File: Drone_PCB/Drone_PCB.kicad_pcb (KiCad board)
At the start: 2 copper layers, 36.2 x 36.2 mm, 53 parts, among them J1 Conn_01x02, J2 Conn_01x02, J3 Conn_01x02, J4 Conn_01x02, J5 USB_B_Mini, J6 Conn_01x05, J7 Conn_01x05, J8 Conn_01x05, J9 Conn_01x02, Q1 TRANS_NPN-MMBT2222AL, Q2 TRANS_NPN-MMBT2222AL, U1 ESP32-WROOM-32, U2 CP2104, U3 SI2302-TP, U4 MIC5219-3.3YMM, U5 SI2302-TP, U6 MPU-6050, U8 SI2302-TP, U9 SI2302-TP

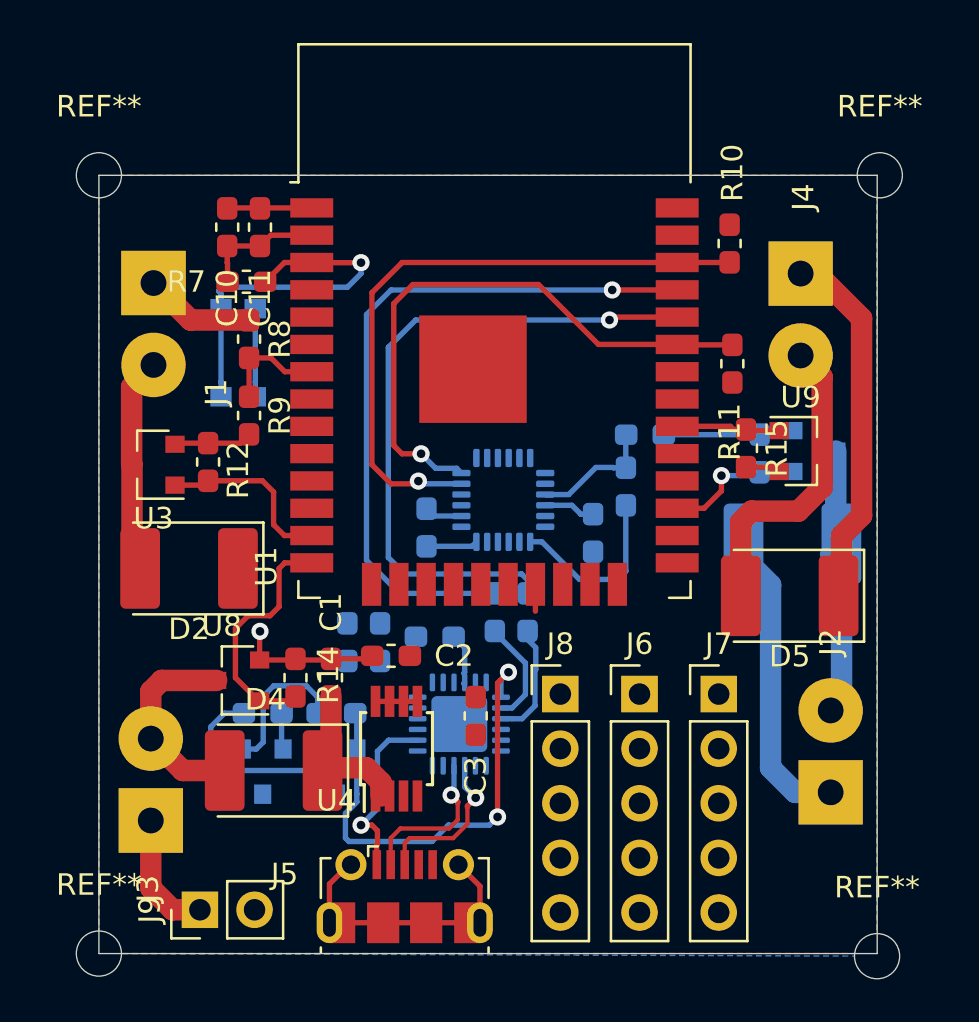
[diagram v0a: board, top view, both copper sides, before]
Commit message: Routing Part 6
We made the tracks thicker and removed some components
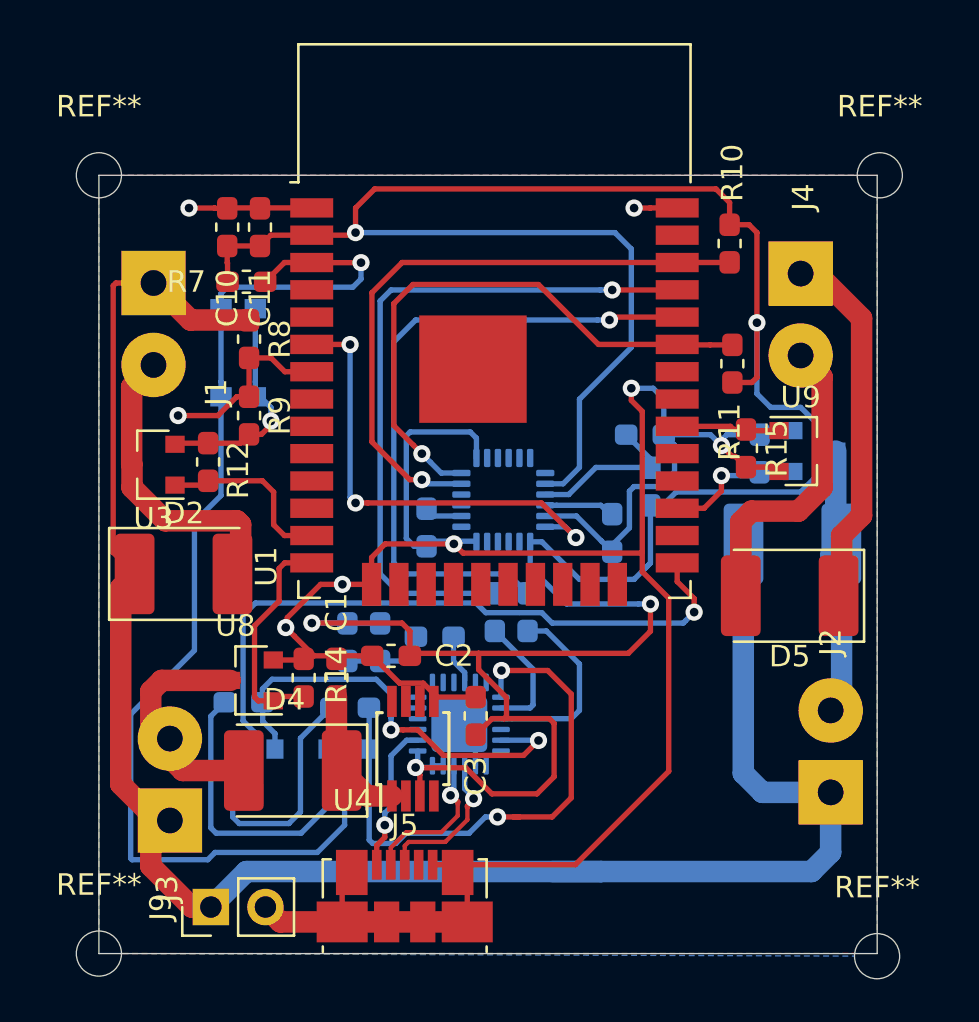
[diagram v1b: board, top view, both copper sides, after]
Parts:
- removed J6, J7, J8: Conn_01x05, Connector_PinHeader_2.54mm:PinHeader_1x05_P2.54mm_Vertical
- J5: footprint Connector_USB:USB_Micro-B_Molex-105017-0001 -> Connector_USB:USB_Micro-B_Molex_47346-0001
- moved R16 1.14 mm to (76.2, 53.5)
- moved R4 1.02 mm to (57.3, 63.5)
- moved D4 0.89 mm to (59.6, 66.7)
- moved C12 0.89 mm to (74.4, 55.6)
- moved J3 0.89 mm to (53.8, 69.0)
- moved U4 0.76 mm to (65.2, 65.7)
- moved R3 0.68 mm to (62.2, 63.8)
- moved U8 0.63 mm to (57.7, 62.5)
- moved J9 0.52 mm to (55.8, 73.0)
- moved Q2 0.51 mm to (62.1, 66.7)
- moved Q1 0.38 mm to (57.8, 66.7)
- moved R14 0.38 mm to (60.1, 62.4)
- moved D2 0.36 mm to (54.5, 57.5), turned to 0 degrees
- moved C1 0.25 mm to (61.6, 62.4)
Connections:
- U1 pad 25: Net-(U1-Pad25) -> /GPIO0
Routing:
- net +3V3: track 14.2 -> 141.2 mm, vias 0 -> 5
- net GND: track 42.5 -> 145.2 mm, vias 1 -> 8
- net V_BATT: track 49.5 -> 113.6 mm
- net /RESET: track 17.3 -> 52.5 mm
- net /GPIO0: track 0.00 -> 32.9 mm, vias 0 -> 1
- net /INT: track 0.00 -> 21.8 mm, vias 0 -> 3
- net /DTR: track 1.70 -> 20.5 mm, vias 0 -> 2
- net Net-(Q2-Pad1): track 8.95 -> 16.2 mm
- net Net-(Q1-Pad1): track 6.93 -> 12.5 mm
- net /RTS: track 21.9 -> 26.6 mm
- net /M1-: track 11.4 -> 16.1 mm
- net /V_BAT_Measure: track 4.99 -> 8.65 mm, vias 0 -> 1
- net /TX_CP2104: track 5.48 -> 9.02 mm
- net /AD0: track 5.82 -> 7.45 mm
- net VBUS: track 8.30 -> 6.88 mm
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
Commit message: Routed completed Ready to order I hope
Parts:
- moved C2 10.7 mm to (74.4, 64.1), turned to 90 degrees
- moved R5 6.95 mm to (77.3, 60.5)
- moved R6 6.95 mm to (75.8, 60.5)
- moved C1 6.49 mm to (67.2, 65.7)
- moved R4 5.50 mm to (62.7, 64.1)
- moved J5 4.96 mm to (69.7, 72.5)
- moved U4 4.83 mm to (70.0, 65.8)
- moved Q1 4.83 mm to (62.6, 66.8)
- moved U2 4.83 mm to (72.1, 64.6)
- moved C3 4.70 mm to (72.8, 64.1)
- moved R3 4.21 mm to (66.4, 64.1)
- moved Q2 4.19 mm to (66.3, 66.8)
- moved R16 3.47 mm to (74.5, 50.4), turned to 0 degrees
- moved J9 2.91 mm to (58.6, 73.3)
- moved J2 2.42 mm to (82.5, 69.0)
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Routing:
- net GND: track 145.2 -> 166.3 mm, vias 8 -> 11
- net /RTS: track 26.6 -> 12.7 mm, vias 2 -> 0
- net /RX_ESP32: track 30.8 -> 17.5 mm
- net /TX_ESP32: track 32.4 -> 19.6 mm
- net /DTR: track 20.5 -> 31.8 mm, vias 2 -> 0
- net +3V3: track 141.2 -> 131.3 mm, vias 5 -> 4
- net Net-(Q2-Pad1): track 16.2 -> 6.80 mm
- net /RESET: track 52.5 -> 44.3 mm, vias 1 -> 3
- net Net-(C7-Pad1): track 2.25 -> 8.49 mm, vias 0 -> 2
- net /M3_PWM: track 10.5 -> 5.07 mm
- net Net-(Q1-Pad1): track 12.5 -> 8.23 mm
- net /SDA: track 27.0 -> 22.8 mm
- net /M1-: track 16.1 -> 11.9 mm
- net /V_BAT_Measure: track 8.65 -> 4.99 mm, vias 1 -> 0
- net /M4-: track 14.4 -> 10.9 mm
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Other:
- board text added: "+"
- board text added: "-"
- board text added: "M1"
- board text added: "M2"
- board text added: "M3"
- board text added: "M4"

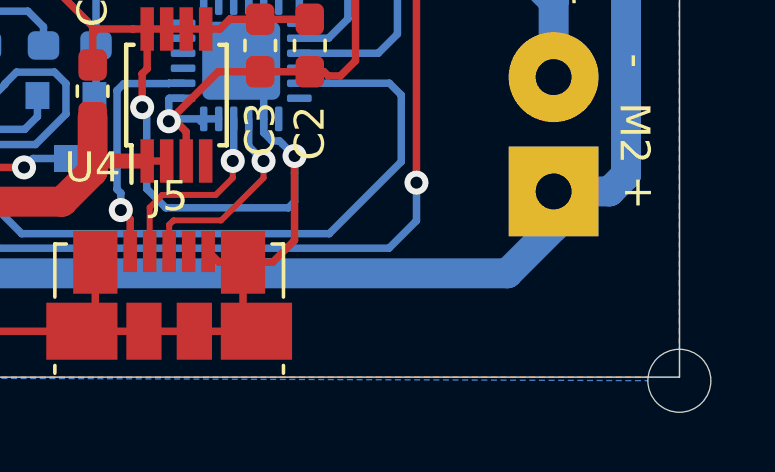
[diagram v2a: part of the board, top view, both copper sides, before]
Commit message: updated drone and battery charger
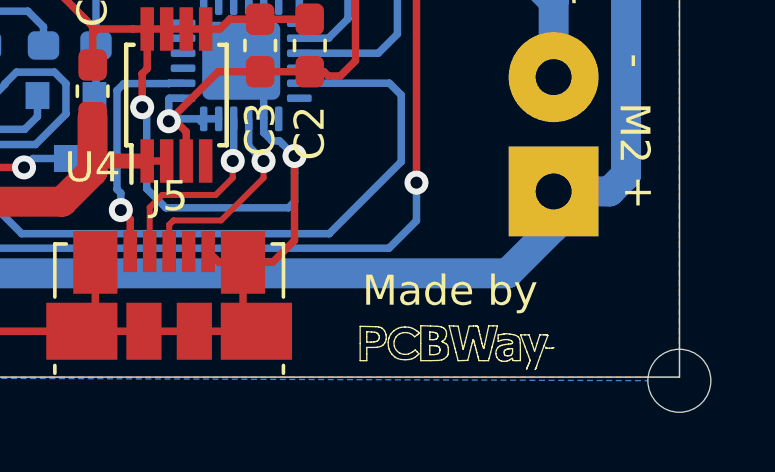
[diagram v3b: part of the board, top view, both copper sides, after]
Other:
- board text added: "Made by"
